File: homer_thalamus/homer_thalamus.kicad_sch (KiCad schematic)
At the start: 20 parts, among them J1 GPIO, J2 MotDrv_Pow_Conn, J3 Right_Motor_Conn, J4 Left_Motor_Conn, J5 Spare_GP_Conn, J6 VBUS_Conn, SW1 SW_PULLDOWN, U1 DRV8874_CARRIER_RIGHT, U2 DRV8874_CARRIER_LEFT, U3 HC-SR04

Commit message: update pcb layout
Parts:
- removed ACC1: GY-521, GY-521:GY-521, symbol GY-521:GY-521
- added U4: HiLetGo-GY-521, GY-521:HiLetGo-GY-521, symbol GY-521:HiLetGo-GY-521
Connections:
- net 3V3(OUT): now also U4.1 (VCC)
- net GND: now also U4.2 (GND)
- net I2C0_SCL: now also U4.3 (SCL)
- net I2C0_SDA: now also U4.4 (SDA)
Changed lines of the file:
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@@
 	)
 	(no_connect
-		(at 58.42 111.76)
+		(at 68.58 111.76)
 	)
 	(no_connect
@@
 	)
 	(no_connect
-		(at 58.42 109.22)
+		(at 68.58 109.22)
 	)
 	(no_connect
@@
 	)
 	(no_connect
-		(at 58.42 104.14)
+		(at 68.58 104.14)
 	)
 	(no_connect
@@
 	)
 	(no_connect
-		(at 58.42 106.68)
+		(at 68.58 106.68)
 	)
 	(no_connect
@@
 	(wire
 		(pts
-			(xy 58.42 96.52) (xy 49.53 96.52)
-		)
-		(stroke
-			(width 0)
-			(type default)
-		)
-	)
-	(wire
-		(pts
 			(xy 63.5 53.34) (xy 90.17 53.34)
 		)
@@
 	(wire
 		(pts
-			(xy 49.53 96.52) (xy 49.53 115.57)
-		)
-		(stroke
-			(width 0)
-			(type default)
-		)
-	)
-	(wire
-		(pts
 			(xy 21.59 60.96) (xy 50.8 60.96)
 		)
@@
 	(wire
 		(pts
-			(xy 36.83 99.06) (xy 58.42 99.06)
+			(xy 46.99 99.06) (xy 68.58 99.06)
 		)
 		(stroke
@@
 	(wire
 		(pts
+			(xy 80.01 119.38) (xy 80.01 121.92)
+		)
+		(stroke
+			(width 0)
+			(type default)
+		)
+	)
+	(wire
+		(pts
 			(xy 45.72 21.59) (xy 45.72 25.4)
 		)
@@
 	(wire
 		(pts
-			(xy 36.83 101.6) (xy 58.42 101.6)
+			(xy 46.99 101.6) (xy 68.58 101.6)
 		)
 		(stroke
@@
 	(wire
 		(pts
+			(xy 80.01 88.9) (xy 80.01 91.44)
+		)
+		(stroke
+			(width 0)
+			(type default)
+		)
+	)
+	(wire
+		(pts
 			(xy 43.18 172.72) (xy 43.18 175.26)
 		)
@@
 	(wire
 		(pts
-			(xy 53.34 93.98) (xy 58.42 93.98)
-		)
-		(stroke
-			(width 0)
-			(type default)
-		)
-	)
-	(wire
-		(pts
 			(xy 21.59 68.58) (xy 50.8 68.58)
 		)
@@
 	(wire
 		(pts
-			(xy 53.34 91.44) (xy 53.34 93.98)
-		)
-		(stroke
-			(width 0)
-			(type default)
-		)
-	)
-	(wire
-		(pts
 			(xy 83.82 153.67) (xy 100.33 153.67)
 		)
@@
 	)
 	(label "I2C0_SDA"
-		(at 36.83 101.6 0)
+		(at 46.99 101.6 0)
 		(effects
 			(font
@@
 	)
 	(label "I2C0_SCL"
-		(at 36.83 99.06 0)
+		(at 46.99 99.06 0)
 		(effects
 			(font
@@
 		(lib_name "GND_1")
 		(lib_id "power:GND")
-		(at 49.53 115.57 0)
+		(at 80.01 121.92 0)
 		(unit 1)
 		(exclude_from_sim no)
@@
 		(fields_autoplaced yes)
 		(property "Reference" "#PWR025"
-			(at 49.53 121.92 0)
+			(at 80.01 128.27 0)
 			(effects
 				(font
@@
 		)
 		(property "Value" "GND"
-			(at 49.53 120.65 0)
+			(at 80.01 127 0)
 			(effects
 				(font
@@
 		)
 		(property "Footprint" ""
-			(at 49.53 115.57 0)
+			(at 80.01 121.92 0)
 			(effects
 				(font
@@
 		)
 		(property "Datasheet" ""
-			(at 49.53 115.57 0)
+			(at 80.01 121.92 0)
 			(effects
 				(font
@@
 		)
 		(property "Description" "Power symbol creates a global label with name \"GND\" , ground"
-			(at 49.53 115.57 0)
+			(at 80.01 121.92 0)
 			(effects
 				(font
@@
 	)
 	(symbol
+		(lib_id "GY-521:HiLetGo-GY-521")
+		(at 80.01 105.41 0)
+		(unit 1)
+		(exclude_from_sim no)
+		(in_bom yes)
+		(on_board yes)
+		(dnp no)
+		(fields_autoplaced yes)
+		(property "Reference" "U4"
+			(at 87.63 104.1399 0)
+			(effects
+				(font
+					(size 1.27 1.27)
+				)
+				(justify left)
+			)
+		)
+		(property "Value" "HiLetGo-GY-521"
+			(at 87.63 106.6799 0)
+			(effects
+				(font
+					(size 1.27 1.27)
+				)
+				(justify left)
+			)
+		)
+		(property "Footprint" "GY-521:HiLetGo-GY-521"
+			(at 81.28 105.41 0)
+			(effects
+				(font
+					(size 1.27 1.27)
+				)
+				(hide yes)
+			)
+		)
+		(property "Datasheet" ""
+			(at 81.28 105.41 0)
+			(effects
+				(font
+					(size 1.27 1.27)
+				)
+				(hide yes)
+			)
+		)
+		(property "Description" ""
+			(at 81.28 105.41 0)
+			(effects
+				(font
+					(size 1.27 1.27)
+				)
+				(hide yes)
+			)
+		)
+		(pin "2"
+		)
+		(pin "8"
+		)
+		(pin "1"
+		)
+		(pin "6"
+		)
+		(pin "4"
+		)
+		(pin "3"
+		)
+		(pin "5"
+		)
+		(pin "7"
+		)
+		(instances
+			(project ""
+				(path "/e63e39d7-6ac0-4ffd-8aa3-1841a4541b55"
+					(reference "U4")
+					(unit 1)
+				)
+			)
+		)
+	)
+	(symbol
 		(lib_name "GND_1")
 		(lib_id "power:GND")
@@
 	(symbol
 		(lib_id "power:+3V3")
-		(at 53.34 91.44 0)
+		(at 80.01 88.9 0)
 		(unit 1)
 		(exclude_from_sim no)
@@
 		(fields_autoplaced yes)
 		(property "Reference" "#PWR024"
-			(at 53.34 95.25 0)
+			(at 80.01 92.71 0)
 			(effects
 				(font
@@
 		)
 		(property "Value" "3V3(OUT)"
-			(at 53.34 86.36 0)
+			(at 80.01 83.82 0)
 			(effects
 				(font
@@
 		)
 		(property "Footprint" ""
-			(at 53.34 91.44 0)
+			(at 80.01 88.9 0)
 			(effects
 				(font
@@
 		)
 		(property "Datasheet" ""
-			(at 53.34 91.44 0)
+			(at 80.01 88.9 0)
 			(effects
 				(font
@@
 		)
 		(property "Description" "Power symbol creates a global label with name \"+3V3\""
-			(at 53.34 91.44 0)
+			(at 80.01 88.9 0)
 			(effects
 				(font
@@
 					(unit 1)
 				)
-			)
-		)
-	)
-	(symbol
-		(lib_id "GY-521:GY-521")
-		(at 74.93 102.87 0)
-		(unit 1)
-		(exclude_from_sim no)
-		(in_bom yes)
-		(on_board yes)
-		(dnp no)
-		(fields_autoplaced yes)
-		(property "Reference" "ACC1"
-			(at 82.55 101.5999 0)
-			(effects
-				(font
-					(size 1.27 1.27)
-				)
-				(justify left)
-			)
-		)
-		(property "Value" "GY-521"
-			(at 82.55 104.1399 0)
-			(effects
-				(font
-					(size 1.27 1.27)
-				)
-				(justify left)
-			)
-		)
-		(property "Footprint" "GY-521:GY-521"
-			(at 74.93 102.87 0)
-			(effects
-				(font
-					(size 1.27 1.27)
-				)
-				(hide yes)
-			)
-		)
-		(property "Datasheet" ""
-			(at 74.93 102.87 0)
-			(effects
-				(font
-					(size 1.27 1.27)
-				)
-				(hide yes)
-			)
-		)
-		(property "Description" ""
-			(at 74.93 102.87 0)
-			(effects
-				(font
-					(size 1.27 1.27)
-				)
-				(hide yes)
-			)
-		)
-		(property "MF" "GODREAM FORDREAM CO., LIMITED"
-			(at 74.93 102.87 0)
-			(effects
-				(font
-					(size 1.27 1.27)
-				)
-				(justify bottom)
-				(hide yes)
-			)
-		)
-		(property "Description_1" "Triple Axis Accelerometer Gyro Breakout"
-			(at 74.93 102.87 0)
-			(effects
-				(font
-					(size 1.27 1.27)
-				)
-				(justify bottom)
-				(hide yes)
-			)
-		)
-		(property "Package" "Package"
-			(at 74.93 102.87 0)
-			(effects
-				(font
-					(size 1.27 1.27)
-				)
-				(justify bottom)
-				(hide yes)
-			)
-		)
-		(property "Price" "None"
-			(at 74.93 102.87 0)
-			(effects
-				(font
-					(size 1.27 1.27)
-				)
-				(justify bottom)
-				(hide yes)
-			)
-		)
-		(property "SnapEDA_Link" "https://www.snapeda.com/parts/GY-521/GODREAM+FORDREAM+CO.%252C+LIMITED/view-part/?ref=snap"
-			(at 74.93 102.87 0)
-			(effects
-				(font
-					(size 1.27 1.27)
-				)
-				(justify bottom)
-				(hide yes)
-			)
-		)
-		(property "MP" "GY-521"
-			(at 74.93 102.87 0)
-			(effects
-				(font
-					(size 1.27 1.27)
-				)
-				(justify bottom)
-				(hide yes)
-			)
-		)
-		(property "Availability" "Not in stock"
-			(at 74.93 102.87 0)
-			(effects
-				(font
-					(size 1.27 1.27)
-				)
-				(justify bottom)
-				(hide yes)
-			)
-		)
-		(property "Check_prices" "https://www.snapeda.com/parts/GY-521/GODREAM+FORDREAM+CO.%252C+LIMITED/view-part/?ref=eda"
-			(at 74.93 102.87 0)
-			(effects
-				(font
-					(size 1.27 1.27)
-				)
-				(justify bottom)
-				(hide yes)
-			)
-		)
-		(pin "XCL"
-		)
-		(pin "XDA"
-		)
-		(pin "INT"
-		)
-		(pin "SDA"
-		)
-		(pin "AD0"
-		)
-		(pin "SCL"
-		)
-		(pin "GND"
-		)
-		(pin "VCC"
-		)
-		(instances
-			(project ""
-				(path "/e63e39d7-6ac0-4ffd-8aa3-1841a4541b55"
-					(reference "ACC1")
-					(unit 1)
-				)

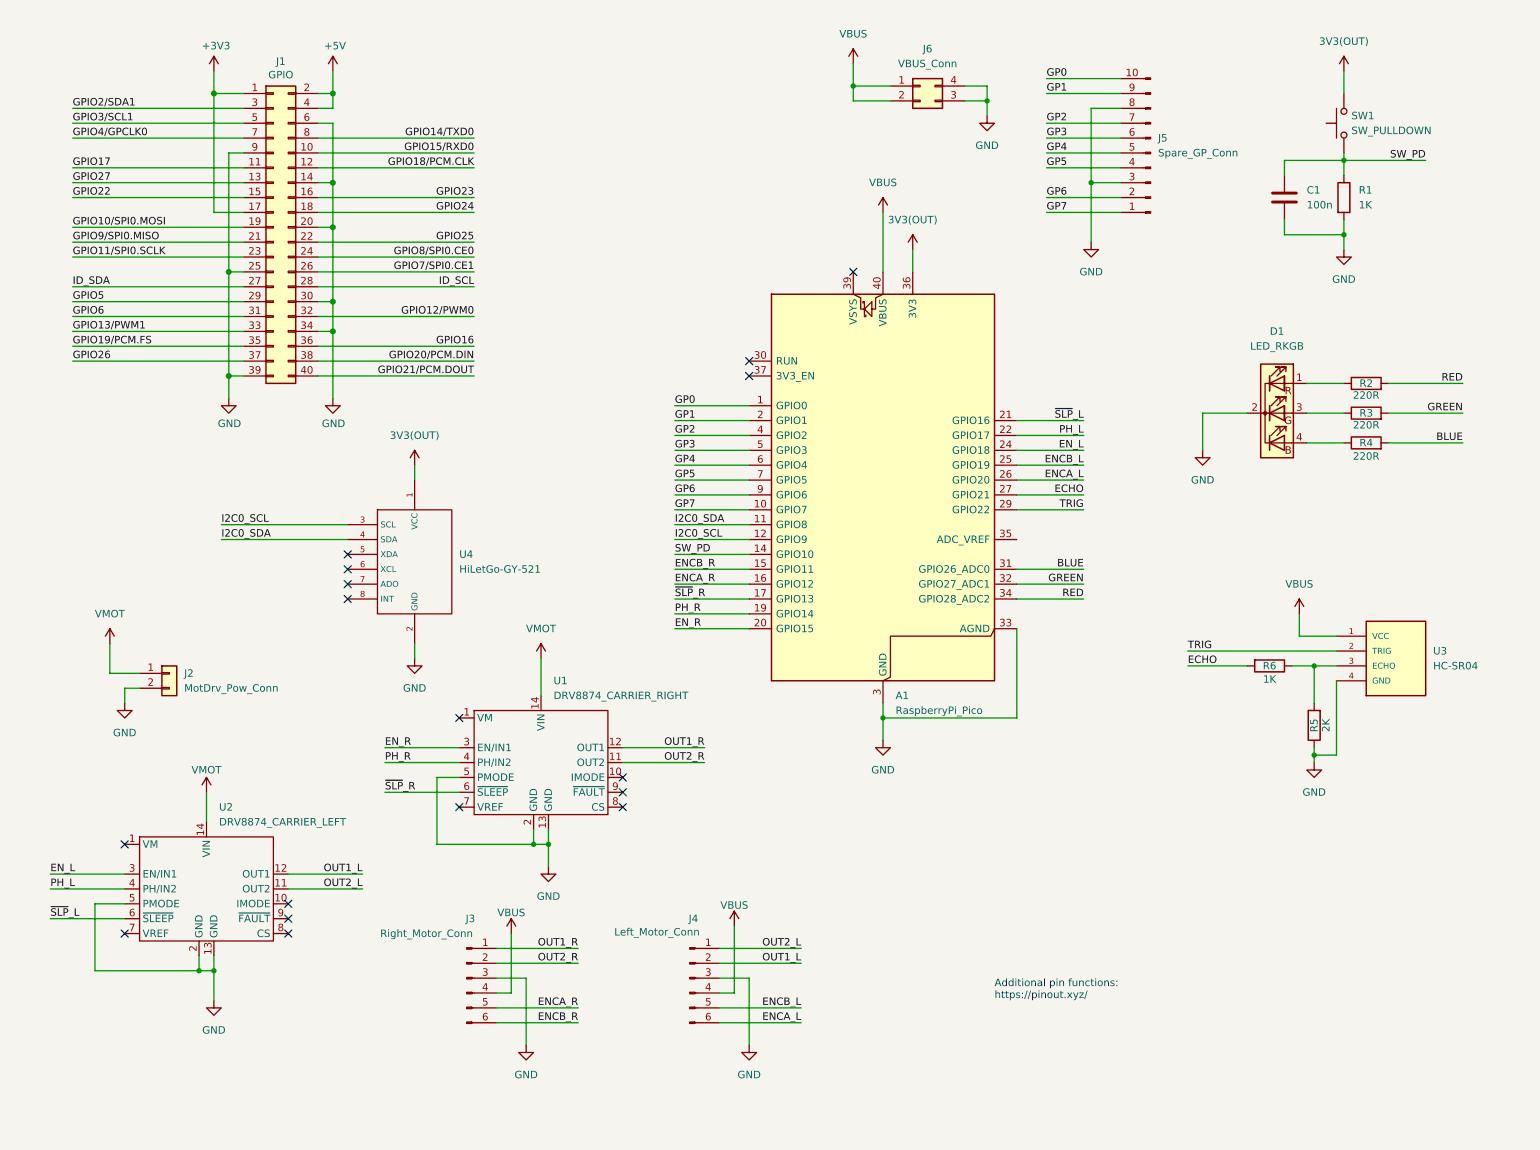
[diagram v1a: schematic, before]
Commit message: route pcb tracks
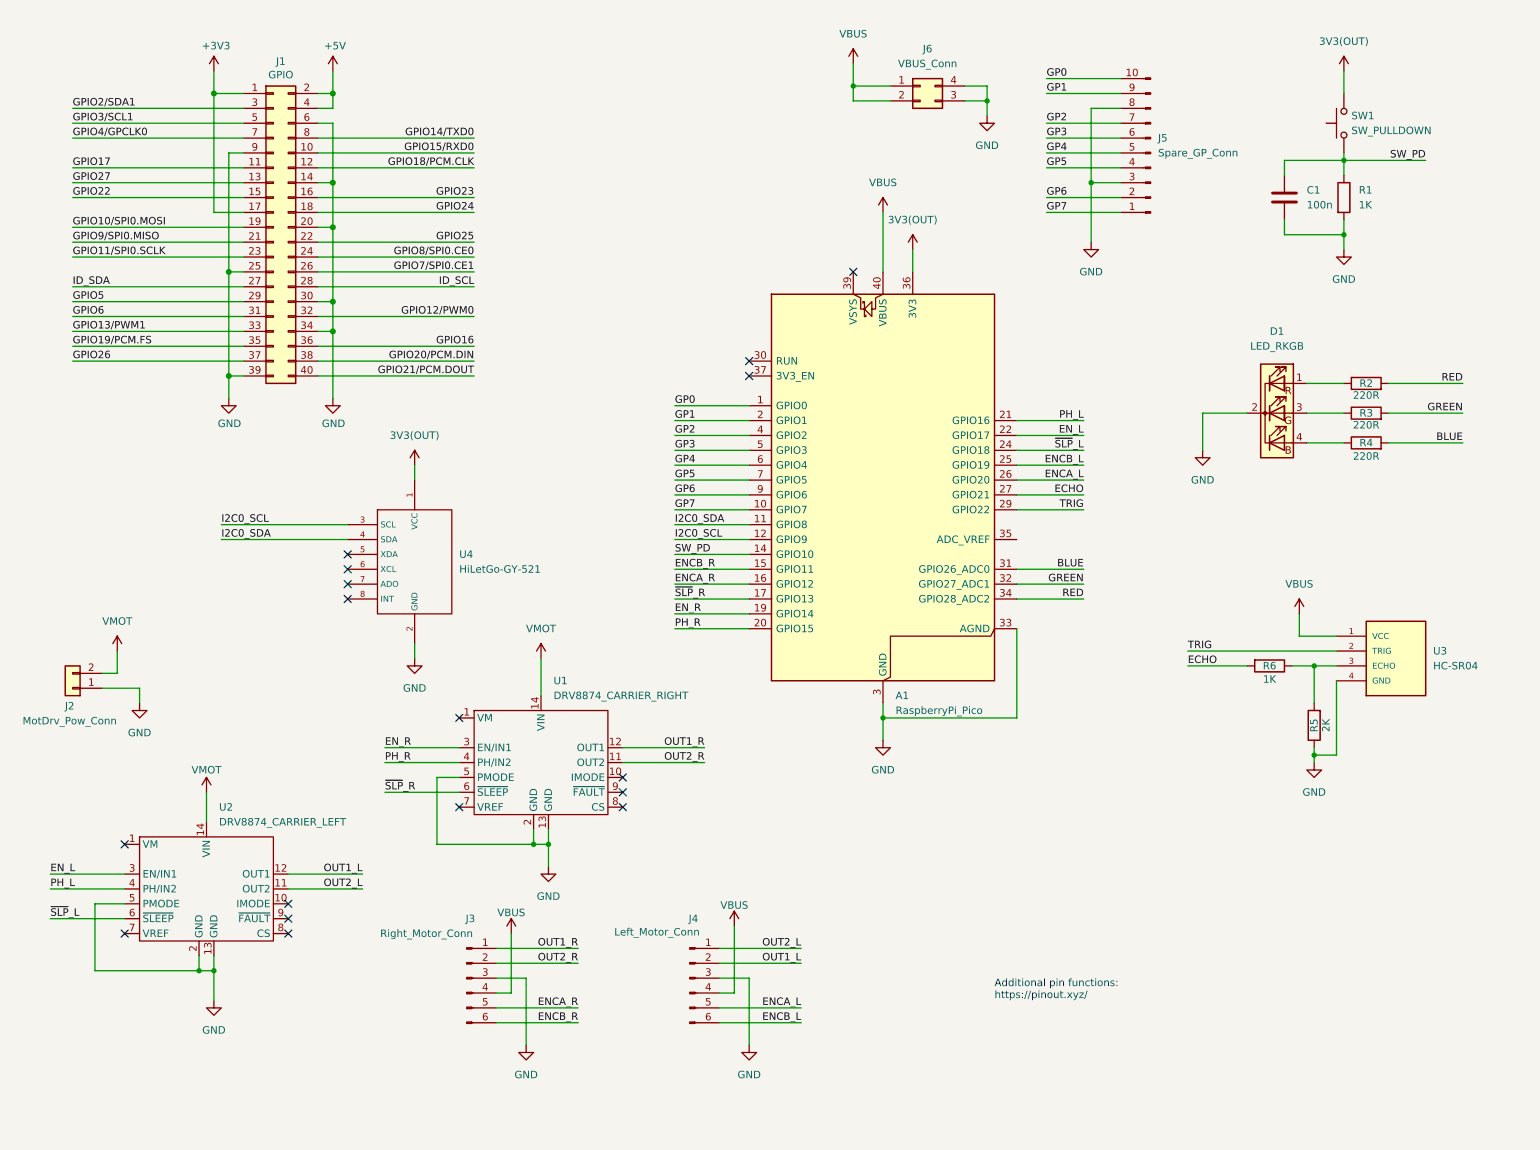
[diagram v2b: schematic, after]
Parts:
- A1: footprint Module:RaspberryPi_Pico_Common_Unspecified -> RaspberryPi_Pico_THT:RaspberryPi_Pico_THT
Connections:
- net ENCA_L: now also J4.5 (Pin_5); no longer J4.6 (Pin_6)
- net ENCB_L: now also J4.6 (Pin_6); no longer J4.5 (Pin_5)
- net EN_L: now also A1.22 (GPIO17); no longer A1.24 (GPIO18)
- net EN_R: now also A1.19 (GPIO14); no longer A1.20 (GPIO15)
- net GND: now also J2.1 (Pin_1); no longer J2.2 (Pin_2)
- net PH_L: now also A1.21 (GPIO16); no longer A1.22 (GPIO17)
- net PH_R: now also A1.20 (GPIO15); no longer A1.19 (GPIO14)
- net VMOT: now also J2.2 (Pin_2); no longer J2.1 (Pin_1)
- net ~{SLP}_L: now also A1.24 (GPIO18); no longer A1.21 (GPIO16)
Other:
- moved on the sheet: J2
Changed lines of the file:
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@@
 	(wire
 		(pts
+			(xy 29.21 124.46) (xy 26.67 124.46)
+		)
+		(stroke
+			(width 0)
+			(type default)
+		)
+	)
+	(wire
+		(pts
 			(xy 187.96 25.4) (xy 200.66 25.4)
 		)
@@
 	(wire
 		(pts
-			(xy 33.02 127) (xy 30.48 127)
-		)
-		(stroke
-			(width 0)
-			(type default)
-		)
-	)
-	(wire
-		(pts
 			(xy 50.8 27.94) (xy 21.59 27.94)
 		)
@@
 	(wire
 		(pts
-			(xy 27.94 119.38) (xy 27.94 124.46)
-		)
-		(stroke
-			(width 0)
-			(type default)
-		)
-	)
-	(wire
-		(pts
 			(xy 45.72 25.4) (xy 45.72 45.72)
 		)
@@
 	(wire
 		(pts
-			(xy 27.94 124.46) (xy 33.02 124.46)
-		)
-		(stroke
-			(width 0)
-			(type default)
-		)
-	)
-	(wire
-		(pts
 			(xy 21.59 68.58) (xy 50.8 68.58)
 		)
@@
 	(wire
 		(pts
-			(xy 30.48 127) (xy 30.48 129.54)
+			(xy 83.82 142.24) (xy 83.82 153.67)
 		)
 		(stroke
@@
 	(wire
 		(pts
-			(xy 83.82 142.24) (xy 83.82 153.67)
+			(xy 233.68 123.19) (xy 237.49 123.19)
 		)
 		(stroke
@@
 	(wire
 		(pts
-			(xy 233.68 123.19) (xy 237.49 123.19)
+			(xy 233.68 138.43) (xy 233.68 139.7)
 		)
 		(stroke
@@
 	(wire
 		(pts
-			(xy 233.68 138.43) (xy 233.68 139.7)
+			(xy 74.93 144.78) (xy 87.63 144.78)
 		)
 		(stroke
@@
 	(wire
 		(pts
-			(xy 74.93 144.78) (xy 87.63 144.78)
+			(xy 212.09 123.19) (xy 222.25 123.19)
 		)
 		(stroke
@@
 	(wire
 		(pts
-			(xy 212.09 123.19) (xy 222.25 123.19)
+			(xy 96.52 179.07) (xy 96.52 168.91)
 		)
 		(stroke
@@
 	(wire
 		(pts
-			(xy 96.52 179.07) (xy 96.52 168.91)
+			(xy 115.57 137.16) (xy 129.54 137.16)
 		)
 		(stroke
@@
 	(wire
 		(pts
-			(xy 115.57 137.16) (xy 129.54 137.16)
+			(xy 29.21 120.65) (xy 29.21 124.46)
 		)
 		(stroke
@@
 	(wire
 		(pts
+			(xy 33.02 127) (xy 33.02 129.54)
+		)
+		(stroke
+			(width 0)
+			(type default)
+		)
+	)
+	(wire
+		(pts
 			(xy 246.38 80.01) (xy 259.08 80.01)
 		)
@@
 	(wire
 		(pts
+			(xy 26.67 127) (xy 33.02 127)
+		)
+		(stroke
+			(width 0)
+			(type default)
+		)
+	)
+	(wire
+		(pts
 			(xy 66.04 66.04) (xy 66.04 77.47)
 		)
@@
 	)
 	(label "~{SLP}_L"
-		(at 194.31 81.28 180)
+		(at 194.31 86.36 180)
 		(effects
 			(font
@@
 	)
 	(label "EN_L"
-		(at 194.31 86.36 180)
+		(at 194.31 83.82 180)
 		(effects
 			(font
@@
 	)
 	(label "PH_L"
-		(at 194.31 83.82 180)
+		(at 194.31 81.28 180)
 		(effects
 			(font
@@
 	)
 	(label "EN_R"
-		(at 124.46 116.84 0)
+		(at 124.46 114.3 0)
 		(effects
 			(font
@@
 	)
 	(label "PH_R"
-		(at 124.46 114.3 0)
+		(at 124.46 116.84 0)
 		(effects
 			(font
@@
 	)
 	(label "ENCB_L"
-		(at 146.05 181.61 180)
+		(at 146.05 184.15 180)
 		(effects
 			(font
@@
 	)
 	(label "ENCA_L"
-		(at 146.05 184.15 180)
+		(at 146.05 181.61 180)
 		(effects
 			(font
@@
 		(lib_name "GND_1")
 		(lib_id "power:GND")
-		(at 30.48 129.54 0)
+		(at 33.02 129.54 0)
 		(unit 1)
 		(exclude_from_sim no)
@@
 		(fields_autoplaced yes)
 		(property "Reference" "#PWR015"
-			(at 30.48 135.89 0)
+			(at 33.02 135.89 0)
 			(effects
 				(font
@@
 		)
 		(property "Value" "GND"
-			(at 30.48 134.62 0)
+			(at 33.02 134.62 0)
 			(effects
 				(font
@@
 		)
 		(property "Footprint" ""
-			(at 30.48 129.54 0)
+			(at 33.02 129.54 0)
 			(effects
 				(font
@@
 		)
 		(property "Datasheet" ""
-			(at 30.48 129.54 0)
+			(at 33.02 129.54 0)
 			(effects
 				(font
@@
 		)
 		(property "Description" "Power symbol creates a global label with name \"GND\" , ground"
-			(at 30.48 129.54 0)
+			(at 33.02 129.54 0)
 			(effects
 				(font
@@
 		(lib_name "+5V_1")
 		(lib_id "power:+5V")
-		(at 27.94 119.38 0)
+		(at 29.21 120.65 0)
 		(unit 1)
 		(exclude_from_sim no)
@@
 		(fields_autoplaced yes)
 		(property "Reference" "#PWR014"
-			(at 27.94 123.19 0)
+			(at 29.21 124.46 0)
 			(effects
 				(font
@@
 		)
 		(property "Value" "VMOT"
-			(at 27.94 114.3 0)
+			(at 29.21 115.57 0)
 			(effects
 				(font
@@
 		)
 		(property "Footprint" ""
-			(at 27.94 119.38 0)
+			(at 29.21 120.65 0)
 			(effects
 				(font
@@
 		)
 		(property "Datasheet" ""
-			(at 27.94 119.38 0)
+			(at 29.21 120.65 0)
 			(effects
 				(font
@@
 		)
 		(property "Description" "Power symbol creates a global label with name \"+5V\""
-			(at 27.94 119.38 0)
+			(at 29.21 120.65 0)
 			(effects
 				(font
@@
 			)
 		)
-		(property "Footprint" "Module:RaspberryPi_Pico_Common_Unspecified"
+		(property "Footprint" "RaspberryPi_Pico_THT:RaspberryPi_Pico_THT"
 			(at 160.02 140.97 0)
 			(effects
@@
 	(symbol
 		(lib_id "Connector_Generic:Conn_01x02")
-		(at 38.1 124.46 0)
+		(at 21.59 127 180)
 		(unit 1)
 		(exclude_from_sim no)
@@
 		(on_board yes)
 		(dnp no)
-		(fields_autoplaced yes)
 		(property "Reference" "J2"
-			(at 40.64 124.4599 0)
+			(at 21.082 130.048 0)
 			(effects
 				(font
 					(size 1.27 1.27)
 				)
-				(justify left)
 			)
 		)
 		(property "Value" "MotDrv_Pow_Conn"
-			(at 40.64 126.9999 0)
+			(at 21.082 132.588 0)
 			(effects
 				(font
 					(size 1.27 1.27)
 				)
-				(justify left)
 			)
 		)
 		(property "Footprint" "Connector_JST:JST_XH_B2B-XH-A_1x02_P2.50mm_Vertical"
-			(at 38.1 124.46 0)
+			(at 21.59 127 0)
 			(effects
 				(font
@@
 		)
 		(property "Datasheet" "~"
-			(at 38.1 124.46 0)
+			(at 21.59 127 0)
 			(effects
 				(font
@@
 		)
 		(property "Description" "Generic connector, single row, 01x02, script generated (kicad-library-utils/schlib/autogen/connector/)"
-			(at 38.1 124.46 0)
+			(at 21.59 127 0)
 			(effects
 				(font
